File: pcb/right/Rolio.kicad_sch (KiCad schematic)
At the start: 110 parts, among them Q1 AO3400A, SW4 SW_DIP_x01

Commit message: Check in V1.0
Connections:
- net at BATT1.1 (+): now also SW4.3; no longer SW4.1
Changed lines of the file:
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@@
       (effects (font (size 1.27 1.27)) hide)
     )
-    (pin "1")
+    (pin "3")
     (pin "2")
     (instances

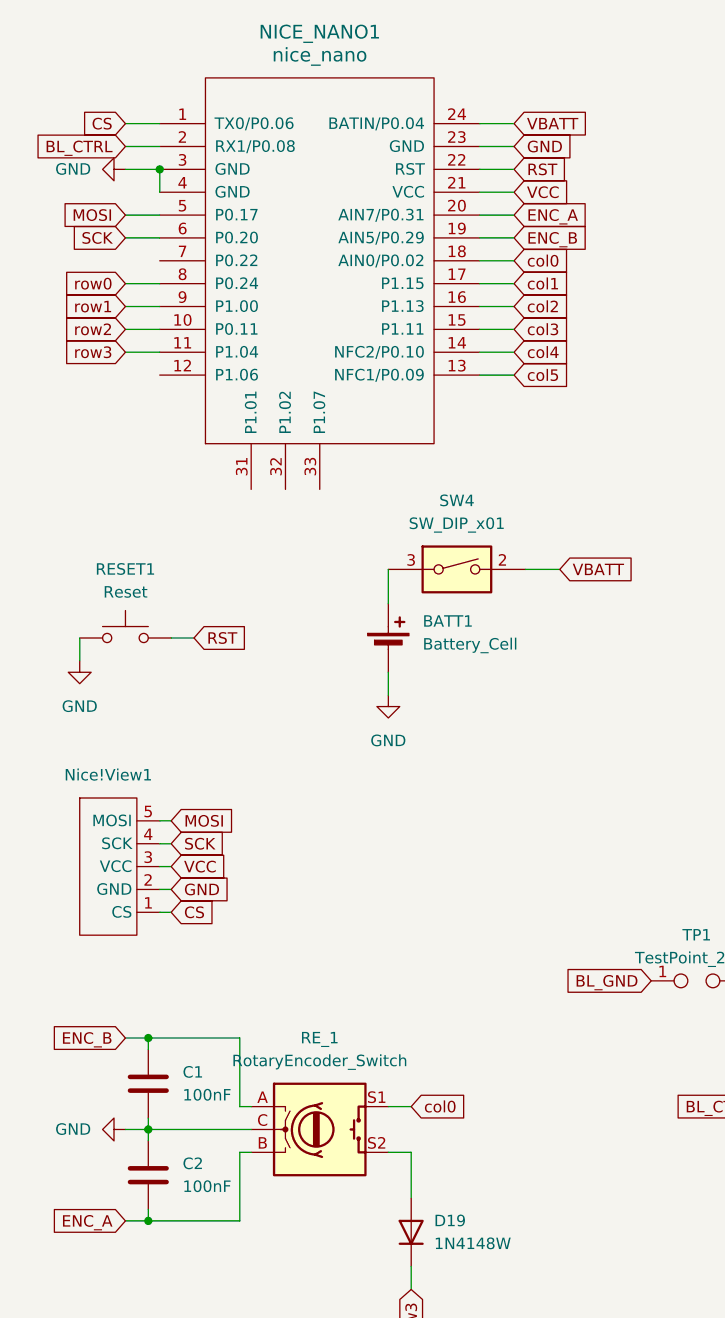
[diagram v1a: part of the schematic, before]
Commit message: Update the right PCB to have a nicer set of solder pads for the battery
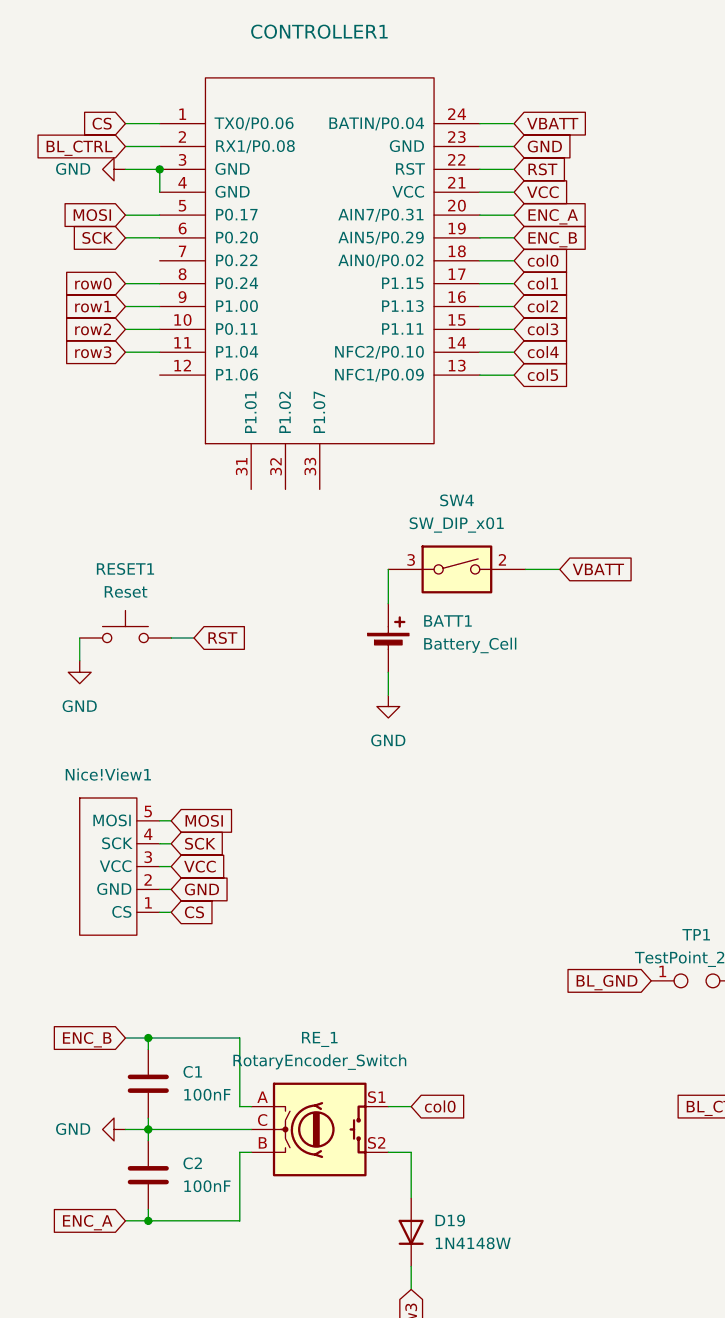
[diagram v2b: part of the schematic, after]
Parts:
- renumbered NICE_NANO1 to CONTROLLER1
